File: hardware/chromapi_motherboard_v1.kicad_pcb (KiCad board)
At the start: 2 copper layers, 140 parts, among them J1 Battery Input, J10 Conn_FSR_TopLeft, J11 Conn_FSR_TopRight, J12 Conn_FSR_BotLeft, J13 Conn_FSR_BotRight, J14 RPI_Connector, J2 Power Switch, J3 USB_C_Receptacle_USB2.0_14P, J4 Conn_ST_STDC14, J5 Conn_TopLeft, J6 Conn_TopRight, J7 Conn_BotLeft, J8 Conn_BotRight, J9 Speaker connector, M1 Noctua NF-A4x10, Q1 PSMN1R5-30YL, Q2 PSMN1R5-30YL, Q3 AO4435, Q4 AO4468, U1 HY2120, U2 CN3302, U3 TPS568230, U4 LD39050PU33R, U5 74AHCT125, U6 STM32G431KBTx, U7 SN74LVC1T45DBV, U8 MAX98357A, U9 BNO055, Y1 32.768k

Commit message: updating component placement
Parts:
- moved J6 49.5 mm to (135.5, 84.5)
- moved J5 45.0 mm to (123.5, 84.5)
- moved J7 34.2 mm to (124.0, 91.5), turned to 180 degrees
- moved J13 33.3 mm to (52.0, 168.0), turned to 0 degrees
- moved J8 30.1 mm to (136.0, 91.5), turned to 180 degrees
- moved C30 25.3 mm to (229.0, 117.5)
- moved C32 25.3 mm to (216.1, 126.6)
- moved C31 25.3 mm to (227.0, 117.5)
- moved C33 25.3 mm to (217.7, 114.0)
- moved C34 25.3 mm to (229.8, 114.0)
- moved FB1 25.3 mm to (226.1, 114.0)
- moved FB2 25.3 mm to (221.4, 114.0)
- moved J9 25.3 mm to (225.0, 110.0)
- moved MK1 25.3 mm to (215.2, 123.5)
- moved R21 25.3 mm to (225.7, 120.7)
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
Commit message: adding 3d models
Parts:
- J1: footprint Connector_JST:JST_XH_B3B-XH-AM_1x03_P2.50mm_Vertical -> Connector_JST:JST_XH_B3B-XH-A_1x03_P2.50mm_Vertical
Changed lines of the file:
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@@
 		)
 		(embedded_fonts no)
+		(model "${KIPRJMOD}/3d_models/INMP441ACEZ_R7.3dshapes/INMP441ACEZ-R7.step"
+			(offset
+				(xyz 0 0 0)
+			)
+			(scale
+				(xyz 1 1 1)
+			)
+			(rotate
+				(xyz -90 -0 -0)
+			)
+		)
 	)
 	(footprint "LED_SMD:LED_0402_1005Metric"
@@
 		)
 		(embedded_fonts no)
-		(model "${KICAD9_3DMODEL_DIR}/Package_DFN_QFN.3dshapes/Texas_RJE0020A_VQFN-20-1EP_3x3mm_P0.45mm_EP0.675x0.76mm.step"
+		(model "${KIPRJMOD}/3d_models/TPS568230RJER.3dshapes/RJE0020B.stp"
 			(offset
 				(xyz 0 0 0)
@@
 		)
 		(embedded_fonts no)
-		(model "${KICAD9_3DMODEL_DIR}/Connector_USB.3dshapes/USB_C_Receptacle_HRO_TYPE-C-31-M-12.step"
+		(model "${KIPRJMOD}/3d_models/TYPE_C_31_M_12.3dshapes/TYPE-C-31-M-12--3DModel-STEP-56544.STEP"
 			(offset
-				(xyz 0 0 0)
+				(xyz 0 -1 0)
 			)
 			(scale
@@
 			)
 			(rotate
-				(xyz 0 0 0)
+				(xyz -90 -0 -0)
 			)
 		)
@@
 		)
 	)
-	(footprint "Connector_JST:JST_XH_B3B-XH-AM_1x03_P2.50mm_Vertical"
+	(footprint "Connector_JST:JST_XH_B3B-XH-A_1x03_P2.50mm_Vertical"
 		(layer "F.Cu")
 		(at 24 31 -90)
-		(descr "JST XH series connector, B3B-XH-AM, with boss (http://www.jst-mfg.com/product/pdf/eng/eXH.pdf), generated with kicad-footprint-generator")
-		(tags "connector JST XH vertical boss")
+		(descr "JST XH series connector, B3B-XH-A (http://www.jst-mfg.com/product/pdf/eng/eXH.pdf), generated with kicad-footprint-generator")
+		(tags "connector JST XH vertical")
 		(property "Reference" "J1"
-			(at 2.5 -3.55 90)
+			(at 2.5 -3.55 270)
 			(layer "F.SilkS")
 			(effects
@@
 		)
 		(property "Value" "Battery Input"
-			(at 2.5 4.6 90)
+			(at 2.5 4.6 270)
 			(layer "F.Fab")
 			(effects
@@
 		)
 		(property "Datasheet" "~"
-			(at 0 0 90)
+			(at 0 0 270)
 			(layer "F.Fab")
 			(hide yes)
@@
 		)
 		(property "Description" "Generic connector, single row, 01x03, script generated (kicad-library-utils/schlib/autogen/connector/)"
-			(at 0 0 90)
+			(at 0 0 270)
 			(layer "F.Fab")
 			(hide yes)
@@
 		(attr through_hole)
 		(fp_line
-			(start 2.5 2.75)
-			(end -0.74 2.75)
+			(start -1.8 2.75)
+			(end 2.5 2.75)
 			(stroke
 				(width 0.12)
@@
 		(fp_line
 			(start -1.8 -0.2)
-			(end -1.8 1.14)
+			(end -1.8 2.75)
 			(stroke
 				(width 0.12)
@@
 		)
 		(fp_text user "${REFERENCE}"
-			(at 2.5 2.7 90)
+			(at 2.5 2.7 270)
 			(layer "F.Fab")
 			(effects
@@
 			)
 		)
-		(pad "" np_thru_hole circle
-			(at -1.6 2 270)
-			(size 1.2 1.2)
-			(drill 1.2)
-			(layers "*.Cu" "*.Mask")
-		)
 		(pad "1" thru_hole roundrect
 			(at 0 0 270)
@@
 		)
 		(embedded_fonts no)
-		(model "${KICAD9_3DMODEL_DIR}/Connector_JST.3dshapes/JST_XH_B3B-XH-AM_1x03_P2.50mm_Vertical.step"
+		(model "${KICAD9_3DMODEL_DIR}/Connector_JST.3dshapes/JST_XH_B3B-XH-A_1x03_P2.50mm_Vertical.step"
 			(offset
 				(xyz 0 0 0)
@@
 		)
 		(embedded_fonts no)
-		(model "${KICAD9_3DMODEL_DIR}/Connector_Molex.3dshapes/Molex_SPOX_5267-03A_1x03_P2.50mm_Vertical.step"
+		(model "${KIPRJMOD}/3d_models/5267_03A_X.3dshapes/5267-03A-X--3DModel-STEP-269445.STEP"
 			(offset
-				(xyz 0 0 0)
+				(xyz 2.5 0.5 0)
 			)
 			(scale
@@
 			)
 			(rotate
-				(xyz 0 0 0)
+				(xyz -90 -0 -0)
 			)
 		)
@@
 		)
 		(embedded_fonts no)
-		(model "${KICAD9_3DMODEL_DIR}/Connector_Molex.3dshapes/Molex_SPOX_5267-03A_1x03_P2.50mm_Vertical.step"
+		(model "${KIPRJMOD}/3d_models/5267_03A_X.3dshapes/5267-03A-X--3DModel-STEP-269445.STEP"
 			(offset
-				(xyz 0 0 0)
+				(xyz 2.5 0.5 0)
 			)
 			(scale
@@
 			)
 			(rotate
-				(xyz 0 0 0)
+				(xyz -90 -0 -0)
 			)
 		)
@@
 		)
 		(embedded_fonts no)
-		(model "${KICAD9_3DMODEL_DIR}/Connector_Molex.3dshapes/Molex_SPOX_5267-03A_1x03_P2.50mm_Vertical.step"
+		(model "${KIPRJMOD}/3d_models/5267_03A_X.3dshapes/5267-03A-X--3DModel-STEP-269445.STEP"
 			(offset
-				(xyz 0 0 0)
+				(xyz 2.5 0.5 0)
 			)
 			(scale
@@
 			)
 			(rotate
-				(xyz 0 0 0)
+				(xyz -90 -0 -0)
 			)
 		)
@@
 		)
 		(embedded_fonts no)
+		(model "${KIPRJMOD}/3d_models/FTSH_107.3dshapes/FTSH-107-01-L-DV-K-A-TR.stp"
+			(offset
+				(xyz 0 0 0.4)
+			)
+			(scale
+				(xyz 1 1 1)
+			)
+			(rotate
+				(xyz -90 -0 -0)
+			)
+		)
 	)
 	(footprint "Resistor_SMD:R_0603_1608Metric"
@@
 		)
 		(embedded_fonts no)
-		(model "${KICAD9_3DMODEL_DIR}/Package_DFN_QFN.3dshapes/TQFN-16-1EP_3x3mm_P0.5mm_EP1.23x1.23mm.step"
+		(model "${KIPRJMOD}/3d_models/MAX98357A.3dshapes/MAX98357AETE+T.STEP"
 			(offset
 				(xyz 0 0 0)
@@
 			)
 			(rotate
-				(xyz 0 0 0)
+				(xyz -90 -0 -0)
 			)
 		)
@@
 		)
 		(embedded_fonts no)
-		(model "${KICAD9_3DMODEL_DIR}/Package_SO.3dshapes/SOP-8_3.76x4.96mm_P1.27mm.step"
+		(model "${KIPRJMOD}/3d_models/SOP8.3dshapes/User Library-sop8_model.STEP"
 			(offset
-				(xyz 0 0 0)
+				(xyz 0 0 1.5)
 			)
 			(scale
@@
 			)
 			(rotate
-				(xyz 0 0 0)
+				(xyz -90 -0 90)
 			)
 		)
@@
 		)
 		(embedded_fonts no)
+		(model "${KIPRJMOD}/3d_models/AO4435.3dshapes/AO4435.step"
+			(offset
+				(xyz 0 0 0)
+			)
+			(scale
+				(xyz 1 1 1)
+			)
+			(rotate
+				(xyz -90 -0 -0)
+			)
+		)
 	)
 	(footprint "TestPoint:TestPoint_Pad_D1.5mm"
@@
 		)
 		(embedded_fonts no)
+		(model "${KIPRJMOD}/3d_models/AO4435.3dshapes/AO4435.step"
+			(offset
+				(xyz 0 0 0)
+			)
+			(scale
+				(xyz 1 1 1)
+			)
+			(rotate
+				(xyz -90 -0 -0)
+			)
+		)
 	)
 	(footprint "Package_TO_SOT_SMD:SOT-23-6"
@@
 		)
 		(embedded_fonts no)
+		(model "${KIPRJMOD}/3d_models/LD39050PU33R.3Dshapes/LD39050PU33R.step"
+			(offset
+				(xyz 0 0 0)
+			)
+			(scale
+				(xyz 1 1 1)
+			)
+			(rotate
+				(xyz -90 -0 -0)
+			)
+		)
 	)
 	(footprint "Inductor_SMD:L_7.3x7.3_H3.5"
@@
 		)
 		(embedded_fonts no)
-		(model "${KICAD9_3DMODEL_DIR}/Inductor_SMD.3dshapes/L_7.3x7.3_H3.5.step"
+		(model "${KIPRJMOD}/3d_models/Inductor_SMD.3dshapes/L_7.3x7.3.STEP"
 			(offset
 				(xyz 0 0 0)
@@
 			)
 			(rotate
-				(xyz 0 0 0)
+				(xyz -90 -0 -0)
 			)
 		)
@@
 		)
 		(embedded_fonts no)
-		(model "${KICAD9_3DMODEL_DIR}/Inductor_SMD.3dshapes/L_7.3x7.3_H3.5.step"
+		(model "${KIPRJMOD}/3d_models/Inductor_SMD.3dshapes/L_7.3x7.3.STEP"
 			(offset
 				(xyz 0 0 0)
@@
 			)
 			(rotate
-				(xyz 0 0 0)
+				(xyz -90 -0 -0)
 			)
 		)
@@
 		)
 		(embedded_fonts no)
-		(model "${KICAD9_3DMODEL_DIR}/Connector_Molex.3dshapes/Molex_SPOX_5267-03A_1x03_P2.50mm_Vertical.step"
+		(model "${KIPRJMOD}/3d_models/5267_03A_X.3dshapes/5267-03A-X--3DModel-STEP-269445.STEP"
+			(offset
+				(xyz 2.5 0.5 0)
+			)
+			(scale
+				(xyz 1 1 1)
+			)
+			(rotate
+				(xyz -90 -0 -0)
+			)
+		)
+		(model " ${KIPRJMOD}/3d_models/5267_03A_X.3dshapes/5267-03A-X--3DModel-STEP-269445.STEP"
 			(offset
 				(xyz 0 0 0)

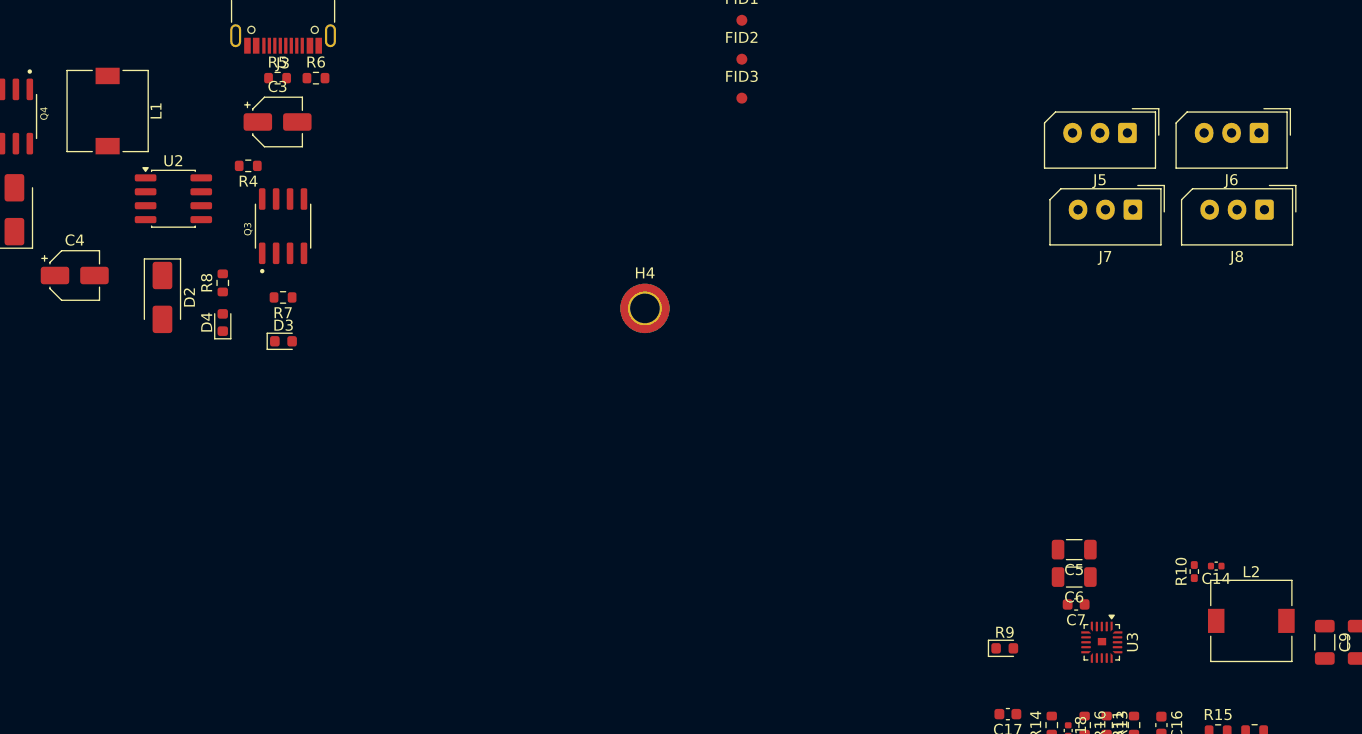
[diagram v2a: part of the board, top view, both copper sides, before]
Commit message: adding inductor 3d model
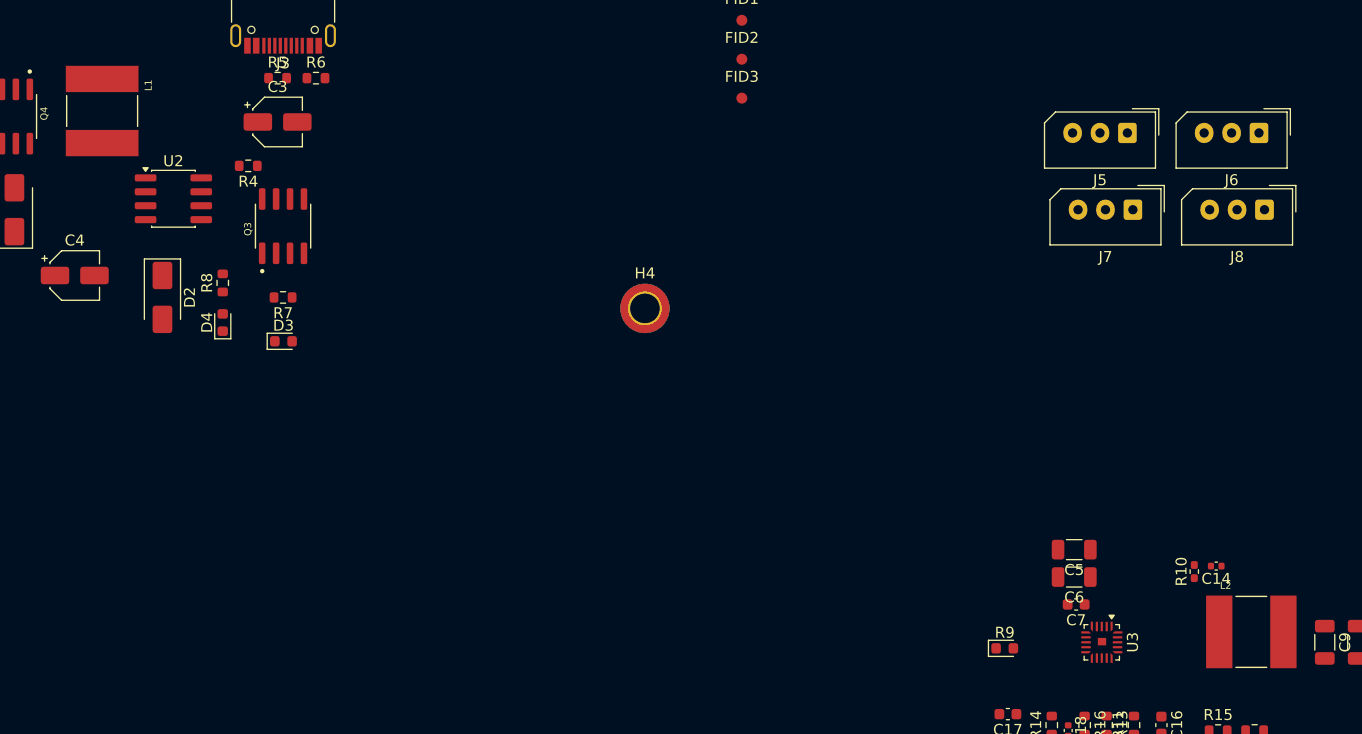
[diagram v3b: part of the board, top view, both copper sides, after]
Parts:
- L1, L2: footprint Inductor_SMD:L_7.3x7.3_H3.5 -> Chromapi_FP:INDM6864X300N
- moved L2 1.00 mm to (134.8, 130.0)
- moved L1 0.50 mm to (30.0, 82.5)
